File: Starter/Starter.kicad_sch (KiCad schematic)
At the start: 66 parts, among them J2 Speaker, J3 UART1, J5 Conn_01x08_Pin, J7 DACOUT, M1 Vibration Motor, Q1 2N2222, SW1 UP, SW2 LEFT, SW3 DOWN, SW4 RIGHT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

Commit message: final sch i think
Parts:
- removed J7: DACOUT, ECE319K:Testpoint_1x02_P2.54mm, symbol ECE319K:Testpoint
- removed JP1: TExaS, ECE319K:PinHeader_1x03_P2.54mm_Vertical, symbol ECE319K:Jumper_3_Open
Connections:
- net DACOUT: now also R11.1, R4.1, R6.1, R7.1, R9.1
- net PA9/PB23: now reaches U2.J1_3 (PA9/PB23)
- net PA9/PB23: now also J5.3 (Pin_3)
- net PB24: now reaches U2.J1_6 (PB24)
- net PB24: now also J5.4 (Pin_4)
- net PB0: now reaches U2.J2_9 (PB0)
- net PB0: now also J5.2 (Pin_2)
- net PB1: now reaches U2.J4_2 (PB1)
- net PB1: now also J5.1 (Pin_1)
- net PA31: now reaches U2.J4_4 (PA31)
- net PA31: now also J5.5 (Pin_5)
- net PA10: now reaches U2.J4_7 (PA10)
- net PA10: now also J5.6 (Pin_6)
- net PA11: now reaches U2.J4_8 (PA11)
- net PA11: now also J5.7 (Pin_7)
- no-connect marks 27 -> 21
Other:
- note removed: "do we even need this?"
- moved on the sheet: R11, R4, R6, R7, R9

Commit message: schematic cleanup
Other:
- note added: "5-Bit DAC"
- note added: "I=(5-1.2-0.5)/220 = 15 mA."
- note added: "IMU"
- note added: "IR Receiver"
- note added: "IR Transmitter"
- note added: "LCD Screen"
- note added: "LED's"
- note added: "MSPM0G3507 LaunchPad"
- note added: "Mounting"
- note added: "Slide Pot"
- note added: "Speaker Amp"
- note added: "Switches"
- note added: "Vibration Motor"
- note removed: "I = (5-1.2-0.5)/220 = 15 mA."
- moved on the sheet: RV1

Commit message: structure changes
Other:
- note added: "Extra"
- moved on the sheet: C5, C6, C7, C8, D1, D2, D3, D5, D6, H1, H2, H3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

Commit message: corrections listed - I'll fix later
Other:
- note added: "Additions: 1.) test points for critical signals (mb ik i fought against UART TX/RX, ADC input, PWM output) 2.) Decoupling caps more? 3.) EEPROM to save high scores even when power is lost - this is a bit of a stretch"
- note added: "Check extra pins are either pulled up/down or left floating as per datasheet"
- note added: "Layout considerations: 1.) GND plane 2.) Short traces on SPI and PWM (high freq) 3.) Separate analog/digital GND planes (noise - is that possible?) 4.) Test points for UART TX/RX, ADC input, PWM (sry ik i fought against it but I changed my mind now) 5.) ergo button placement for easy access when holding board 6.) So tempted to 3d print an enclosure 7.) COPPER NAMES PLEASE, also def black idc how 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"
- note added: "check cap vals for coupling/filtering fit frequency range"
- note added: "check match I2C speed req."
- note added: "check no conflicts arise from shared peripheral (UART pins for both comm and other funcs.)"
- note added: "flyback against back EMF"
- note added: "i like the transistor choice :)"
- note added: "pull up resistors needed for signal integrity? I'll check bc I think just no connects is sufficient tho"
- note added: "yay switch debouncing"
- moved on the sheet: C1, C10, C11, C12, C13, C2, C3, C4, C5, C6, C7, C8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

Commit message: I like my sch structure more :)
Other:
- note added: "pull up for signal integrity? I'll check bc no connects is prob sufficient"
- note removed: "pull up resistors needed for signal integrity? I'll check bc I think just no connects is sufficient tho"
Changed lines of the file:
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@@
 		)
 	)
-	(text "pull up resistors needed\nfor signal integrity?\nI'll check bc I think just no\nconnects is sufficient tho"
+	(text "pull up\nfor signal integrity?\nI'll check bc no connects\nis prob sufficient"
 		(exclude_from_sim no)
 		(at 137.16 106.68 0)

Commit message: brain dumped - I'll clean later
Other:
- note added: "Additions: 1.) test points for critical signals (mb ik i fought against UART TX/RX, ADC input, PWM output) 2.) EEPROM to save high scores even when power is lost - this is a bit of a stretch 3.) More decoupling caps? especially if using EEPROM 4.) Need to go in and change footprints/add mouser details for BOM"
- note added: "Layout considerations: 1.) GND plane 2.) Short traces on SPI and PWM (high freq) 3.) This is a strettch but separate analog/digital GND planes (against noise - is that possible?) 4.) Test points for UART TX/RX, ADC input, PWM (sry ik i fought against it but it would be helpful lol) 5.) ergo button placement for easy access when holding board 6.) So tempted to 3d print an enclosure 7.) can be put 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"
- note added: "double check this pinout"
- note removed: "Additions: 1.) test points for critical signals (mb ik i fought against UART TX/RX, ADC input, PWM output) 2.) Decoupling caps more? 3.) EEPROM to save high scores even when power is lost - this is a bit of a stretch"
- note removed: "Layout considerations: 1.) GND plane 2.) Short traces on SPI and PWM (high freq) 3.) Separate analog/digital GND planes (noise - is that possible?) 4.) Test points for UART TX/RX, ADC input, PWM (sry ik i fought against it but I changed my mind now) 5.) ergo button placement for easy access when holding board 6.) So tempted to 3d print an enclosure 7.) COPPER NAMES PLEASE, also def black idc how 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"
- note removed: "check no conflicts arise from shared peripheral (UART pins for both comm and other funcs.)"
- note removed: "i like the transistor choice :)"
- note removed: "pull up for signal integrity? I'll check bc no connects is prob sufficient"
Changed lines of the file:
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@@
 		)
 	)
-	(text "i like the transistor choice :)"
-		(exclude_from_sim no)
-		(at 321.564 156.718 0)
-		(effects
-			(font
-				(size 1.27 1.27)
-				(color 255 11 18 1)
-			)
-		)
-	)
-	(text "Layout considerations:\n1.) GND plane\n2.) Short traces on SPI and PWM (high freq)\n3.) Separate analog/digital GND planes (noise - is that possible?)\n4.) Test points for UART TX/RX, ADC input, PWM (sry ik i fought against it\nbut I changed my mind now)\n5.) ergo button placement for easy access when holding board\n6.) So tempted to 3d print an enclosure \n7.) COPPER NAMES PLEASE, also def black idc how much it costs"
+	(text "Layout considerations:\n1.) GND plane\n2.) Short traces on SPI and PWM (high freq)\n3.) This is a strettch but separate analog/digital GND planes (against noise - is that possible?)\n4.) Test points for UART TX/RX, ADC input, PWM (sry ik i fought against it\nbut it would be helpful lol)\n5.) ergo button placement for easy access when holding board\n6.) So tempted to 3d print an enclosure \n7.) can be put our names in copper pleaseeee\n8.) we are 100% ordering this in black idc how much it costs"
 		(exclude_from_sim no)
 		(at 67.056 26.416 0)
@@
 		)
 	)
-	(text "flyback against\nback EMF"
-		(exclude_from_sim no)
-		(at 302.006 128.016 0)
+	(text "flyback \nagainst\nback EMF"
+		(exclude_from_sim no)
+		(at 301.244 131.826 0)
 		(effects
 			(font
@@
 		)
 	)
-	(text "check no conflicts arise\nfrom shared peripheral \n(UART pins for both comm and other funcs.)"
-		(exclude_from_sim no)
-		(at 36.576 116.078 0)
-		(effects
-			(font
-				(size 1.27 1.27)
-				(color 255 16 28 1)
-			)
-		)
-	)
 	(text "COM floating"
 		(exclude_from_sim no)
@@
 		)
 	)
-	(text "pull up\nfor signal integrity?\nI'll check bc no connects\nis prob sufficient"
+	(text "double check this pinout"
 		(exclude_from_sim no)
 		(at 137.16 106.68 0)
@@
 		)
 	)
-	(text "Additions:\n1.) test points for critical signals (mb ik i fought against\nUART TX/RX, ADC input, PWM output)\n2.) Decoupling caps more?\n3.) EEPROM to save high\nscores even when power is lost - this is a bit of a stretch"
-		(exclude_from_sim no)
-		(at 68.58 55.626 0)
+	(text "Additions:\n1.) test points for critical signals (mb ik i fought against\nUART TX/RX, ADC input, PWM output)\n2.) EEPROM to save high\nscores even when power is lost - this is a bit of a stretch\n3.) More decoupling caps? especially if using EEPROM\n4.) Need to go in and change footprints/add mouser details for BOM"
+		(exclude_from_sim no)
+		(at 62.992 50.8 0)
 		(effects
 			(font
@@
 	(text "yay switch debouncing"
 		(exclude_from_sim no)
-		(at 205.486 115.062 0)
-		(effects
-			(font
+		(at 206.248 113.792 0)
+		(effects
+			(font

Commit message: final sch? footprint fixes
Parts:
- removed C1: 1uF, symbol ECE319K:C_Polarized
- removed C2: 4.7uF, symbol ECE319K:C_Polarized
- removed J3: UART1, ECE319K:PinHeader_1x03_P2.54mm_Vertical, symbol ECE319K:Header_3
- added C14: 1uF, Capacitor_SMD:C_0603_1608Metric_Pad1.08x0.95mm_HandSolder, symbol ECE319K:C
- added C15: 4.7uF, Capacitor_SMD:C_0603_1608Metric_Pad1.08x0.95mm_HandSolder, symbol ECE319K:C
- C10, C11, C12, C13, C3, C4, C5, C6, C7, C8, C9: footprint (none) -> Capacitor_SMD:C_0603_1608Metric_Pad1.08x0.95mm_HandSolder
- D1, D2, D3, D4, D5, D6: footprint (none) -> LED_SMD:LED_0805_2012Metric
- R1, R10, R11, R12, R13, R14, R15, R16, R17, R18, R19, R2, R20, R21, R22, R23, R24, R3, R4, R5, R6, R7, R8, R9: footprint (none) -> Resistor_SMD:R_0603_1608Metric_Pad0.98x0.95mm_HandSolder
- SW1, SW2, SW3, SW4: footprint (none) -> Button_Switch_SMD:SW_Push_1P1T_NO_6x6mm_H9.5mm; Mouser # (none) -> 506-1977223-1; Mouser Link (none) -> https://www.mouser.com/ProductDetail/TE-Connectivity-PB/197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
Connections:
- net GND: now also C14.1, C15.2
- net at U3.2 (FC2): now also C15.1
- net at U3.3 (FC1): now also C14.2
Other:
- note added: "Additions: 1.) test points for critical signals (mb ik i fought against UART TX/RX, ADC input, PWM output) 2.) SD card 3.) More decoupling caps? 4.) Need to go in and change footprints/add mouser details for BOM"
- note added: "check IMU"
- note removed: "Additions: 1.) test points for critical signals (mb ik i fought against UART TX/RX, ADC input, PWM output) 2.) EEPROM to save high scores even when power is lost - this is a bit of a stretch 3.) More decoupling caps? especially if using EEPROM 4.) Need to go in and change footprints/add mouser details for BOM"
- note removed: "Check extra pins are either pulled up/down or left floating as per datasheet"
- note removed: "Connect the microcontroller pin PA8 to one of the input pins on the ULN2003B"
- note removed: "Layout considerations: 1.) GND plane 2.) Short traces on SPI and PWM (high freq) 3.) This is a strettch but separate analog/digital GND planes (against noise - is that possible?) 4.) Test points for UART TX/RX, ADC input, PWM (sry ik i fought against it but it would be helpful lol) 5.) ergo button placement for easy access when holding board 6.) So tempted to 3d print an enclosure 7.) can be put 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"
- note removed: "add pins and redo resistor vals based on LED datasheet"
- note removed: "check cap vals for coupling/filtering fit frequency range"
- note removed: "double check this pinout"
- note removed: "yay switch debouncing"

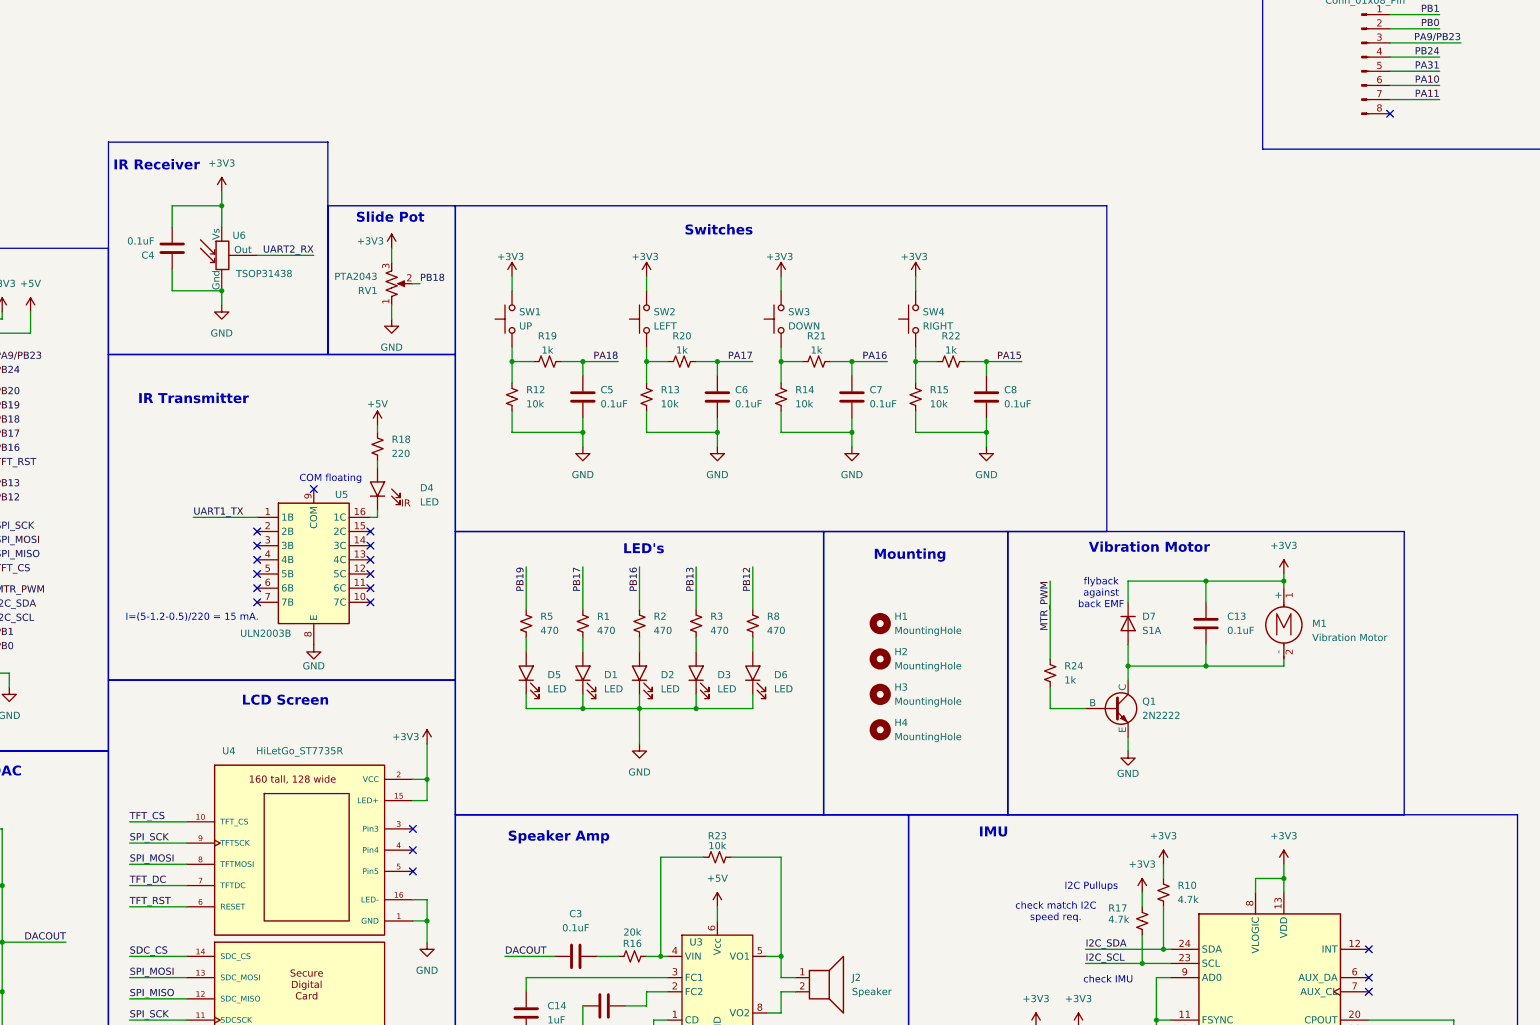
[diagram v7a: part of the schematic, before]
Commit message: need imu
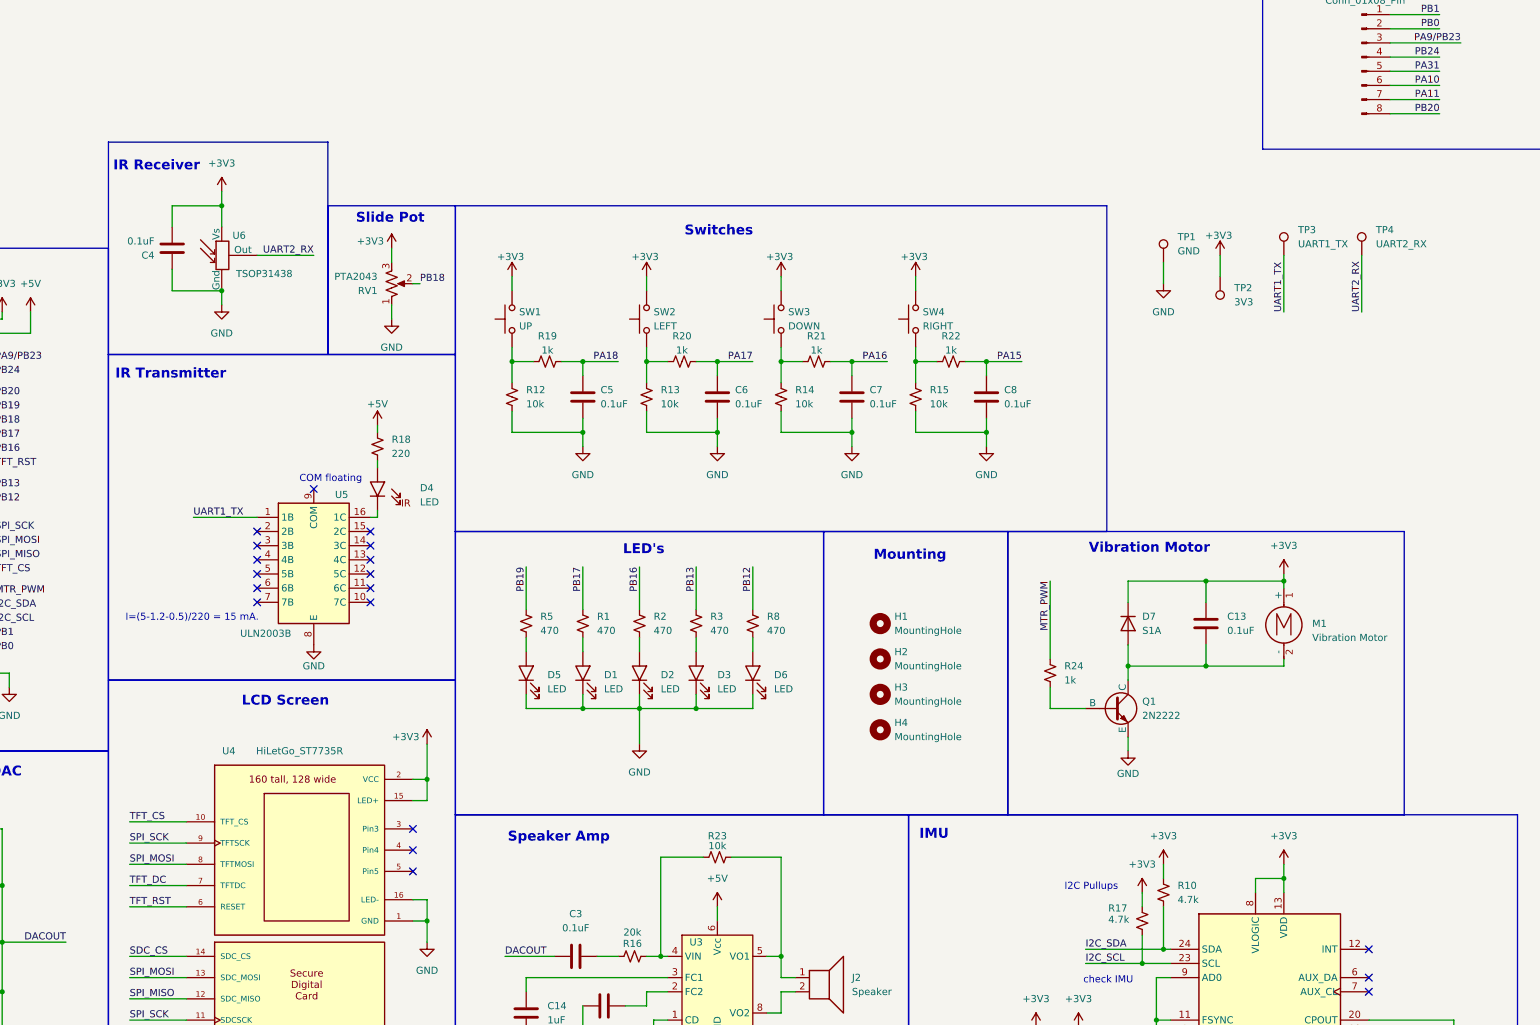
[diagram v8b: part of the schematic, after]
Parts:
- added TP1: GND, TestPoint:TestPoint_Pad_1.0x1.0mm, symbol Connector:TestPoint
- added TP2: 3V3, TestPoint:TestPoint_Pad_1.0x1.0mm, symbol Connector:TestPoint
- added TP3: UART1_TX, TestPoint:TestPoint_Pad_1.0x1.0mm, symbol Connector:TestPoint
- added TP4: UART2_RX, TestPoint:TestPoint_Pad_1.0x1.0mm, symbol Connector:TestPoint
- D7: footprint (none) -> Diode_SMD:D_SMA; Mouser # (none) -> 512-S1A; Mouser Link (none) -> https://www.mouser.com/ProductDetail/onsemi-Fairchild/S1A?q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
- J2: footprint ECE319K:PinHeader_1x02_P2.54mm_Vertical -> Connector_Wire:SolderWirePad_1x01_SMD_1x2mm
- M1: footprint (none) -> Connector_Wire:SolderWirePad_1x01_SMD_1x2mm; Mouser # (none) -> 316040001; Mouser Link (none) -> https://www.mouser.com/ProductDetail/Seeed-Studio/316040001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
- Q1: Mouser # (none) -> MMBT2222A; Mouser Link (none) -> https://www.mouser.com/ProductDetail/Diotec-Semiconductor/M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
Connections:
- net +3V3: now also TP2.1
- net GND: now also TP1.1
- net PB20: now also J5.8 (Pin_8)
- net UART1_TX: now also TP3.1
- net UART2_RX: now also TP4.1
- no-connect marks 21 -> 20
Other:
- note removed: "check match I2C speed req."
- note removed: "flyback against back EMF"
